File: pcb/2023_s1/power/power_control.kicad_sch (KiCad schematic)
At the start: 21 parts, among them J1 Screw_Terminal_01x05, Q2 TIP122, U1 40106, U3 4N25

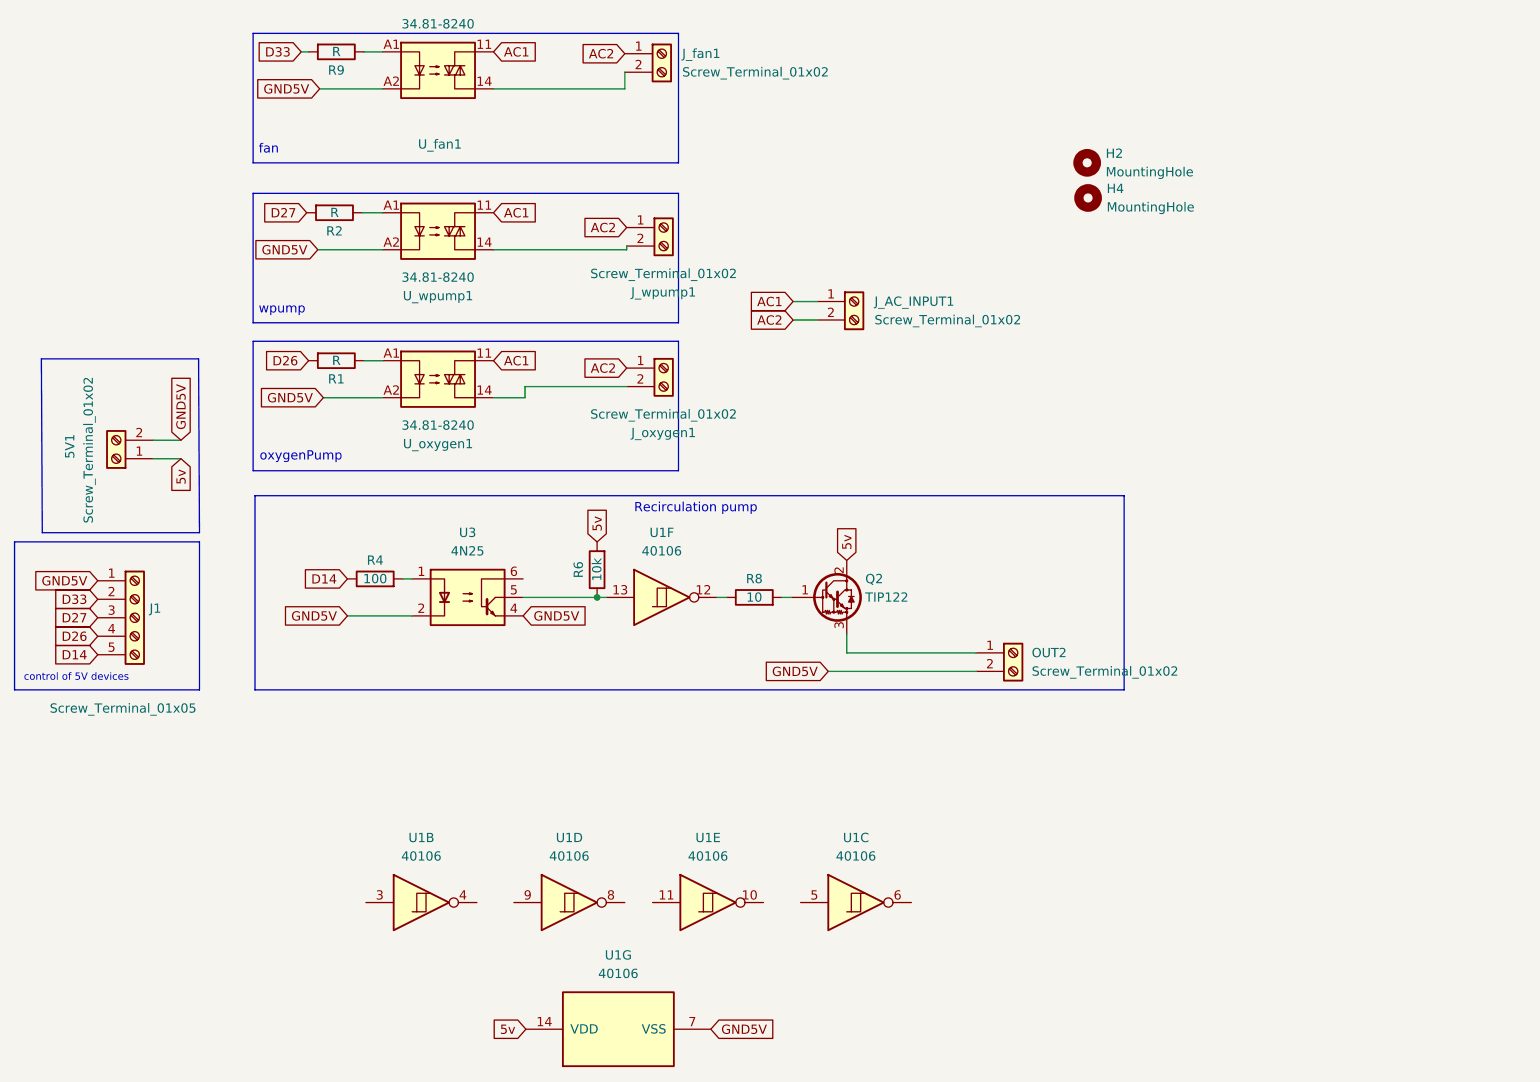
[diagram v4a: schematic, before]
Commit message: update, changed pcbs to use mechanic relays instead of the trigger schmith circuit, because of reliability and simpleness of the design
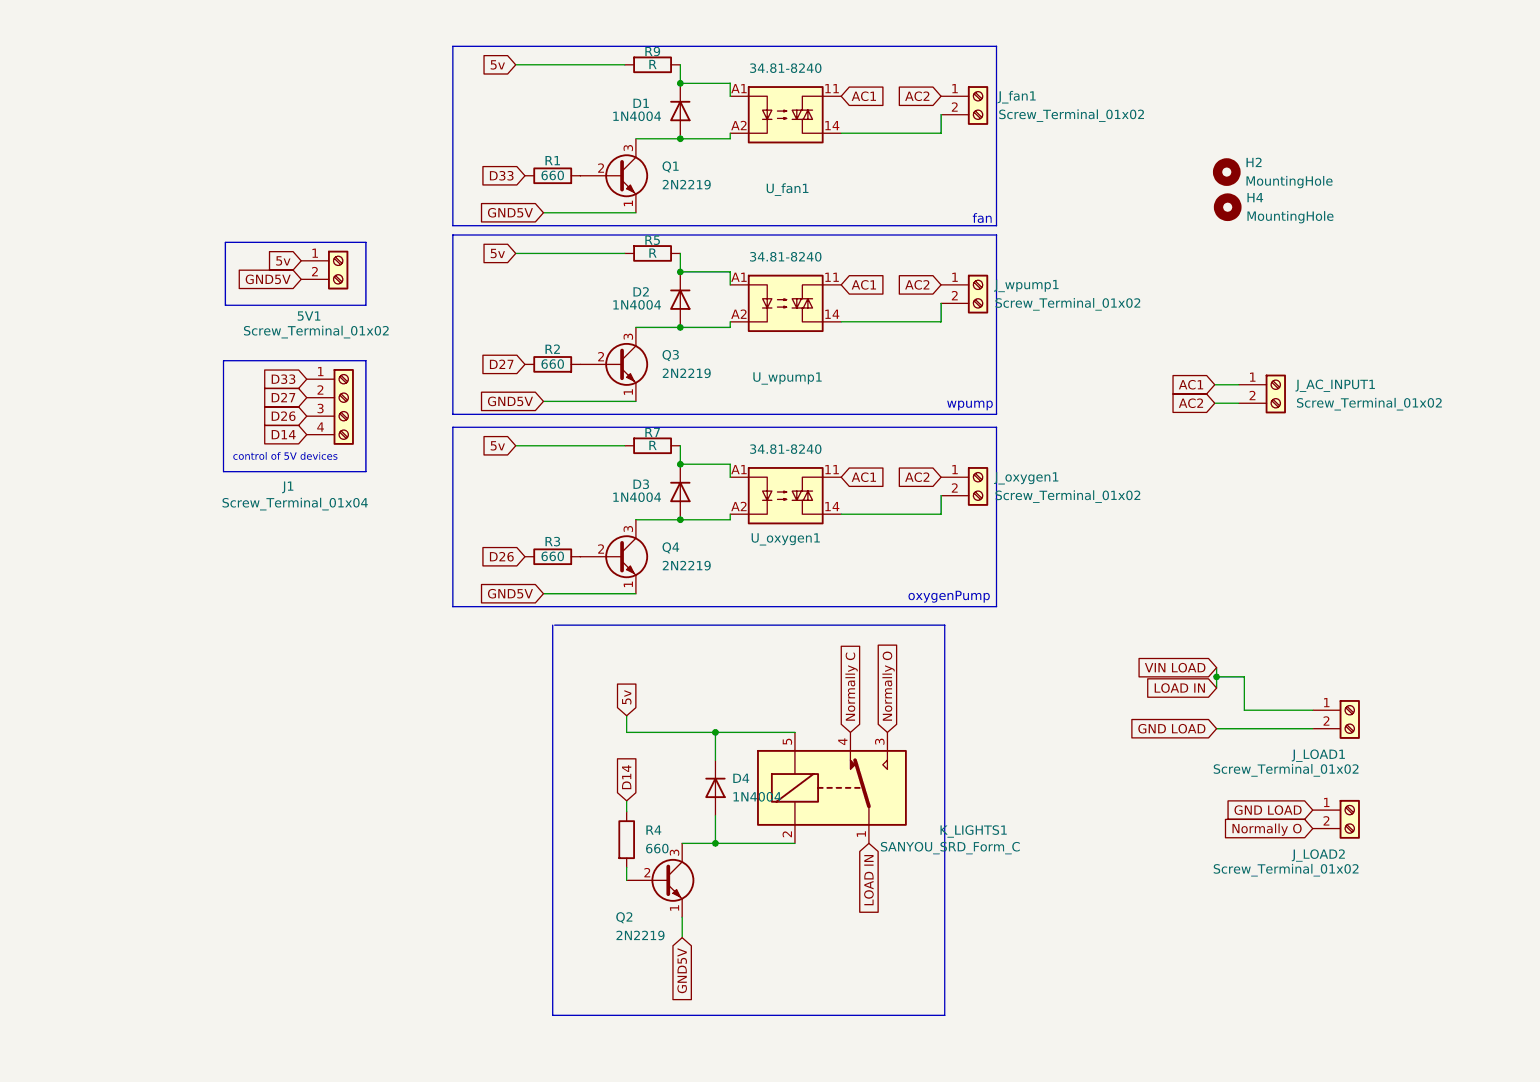
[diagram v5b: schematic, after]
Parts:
- removed J1: Screw_Terminal_01x05, TerminalBlock_Altech:Altech_AK300_1x05_P5.00mm_45-Degree, symbol Connector:Screw_Terminal_01x05
- removed OUT2: Screw_Terminal_01x02, TerminalBlock:TerminalBlock_Altech_AK300-2_P5.00mm, symbol Connector:Screw_Terminal_01x02
- removed Q2: TIP122, Package_TO_SOT_THT:TO-220-3_Vertical, symbol Transistor_BJT:TIP122
- removed R6: 10k, Resistor_THT:R_Axial_DIN0204_L3.6mm_D1.6mm_P2.54mm_Vertical, symbol Device:R
- removed R8: 10, Resistor_THT:R_Axial_DIN0204_L3.6mm_D1.6mm_P2.54mm_Vertical, symbol Device:R
- removed U1: 40106, Package_DIP:DIP-14_W7.62mm, symbol 4xxx:40106
- removed U3: 4N25, Package_DIP:DIP-6_W7.62mm, symbol Isolator:4N25
- added D1, D2, D3, D4: 1N4004, Diode_THT:D_DO-41_SOD81_P10.16mm_Horizontal, symbol Diode:1N4004
- added J1: Screw_Terminal_01x04, TerminalBlock_Altech:Altech_AK300_1x04_P5.00mm_45-Degree, symbol Connector:Screw_Terminal_01x04
- added J_LOAD1, J_LOAD2: Screw_Terminal_01x02, TerminalBlock:TerminalBlock_Altech_AK300-2_P5.00mm, symbol Connector:Screw_Terminal_01x02
- added K_LIGHTS1: SANYOU_SRD_Form_C, Relay_THT:Relay_SPDT_SANYOU_SRD_Series_Form_C, symbol Relay:SANYOU_SRD_Form_C
- added Q1, Q2, Q3, Q4: 2N2219, Package_TO_SOT_THT:TO-39-3, symbol Transistor_BJT:2N2219
- added R3: 660, Resistor_THT:R_Axial_DIN0204_L3.6mm_D1.6mm_P5.08mm_Vertical, symbol Device:R
- added R5, R7: R, Resistor_THT:R_Axial_DIN0204_L3.6mm_D1.6mm_P5.08mm_Vertical, symbol Device:R
- R1, R2: value R -> 660
- R4: value 100 -> 660; footprint Resistor_THT:R_Axial_DIN0204_L3.6mm_D1.6mm_P2.54mm_Vertical -> Resistor_THT:R_Axial_DIN0204_L3.6mm_D1.6mm_P5.08mm_Vertical
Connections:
- net 5v: now also R9.2, D4.1 (K), K_LIGHTS1.5, R5.2, R7.2
- net D14: now also J1.4 (Pin_4)
- net D26: now also J1.3 (Pin_3), R3.1; no longer R1.2
- net D27: now also R2.1, J1.2 (Pin_2); no longer R2.2
- net D33: now also R1.1, J1.1 (Pin_1); no longer R9.2
- net GND5V: now also Q1.1 (E), Q2.1 (E), Q3.1 (E), Q4.1 (E); no longer U_fan1.A2, U_oxygen1.A2, U_wpump1.A2
- net at U_wpump1.A1: now also D2.1 (K), R5.1; no longer R2.1
- net at R9.1, U_fan1.A1: now also D1.1 (K)
- net at U_oxygen1.A1: now also D3.1 (K), R7.1; no longer R1.1
- net at R4.2: now also Q2.2 (B)
- new net: Q3.2 (B), R2.2
- new net: D2.2 (A), Q3.3 (C), U_wpump1.A2
- new net: D3.2 (A), Q4.3 (C), U_oxygen1.A2
- new net: Q1.2 (B), R1.2
- new net: D1.2 (A), Q1.3 (C), U_fan1.A2
- new net: Q4.2 (B), R3.2
- new net: D4.2 (A), K_LIGHTS1.2, Q2.3 (C)
- new net GND LOAD: J_LOAD1.2 (Pin_2), J_LOAD2.1 (Pin_1)
- new net LOAD IN: J_LOAD1.1 (Pin_1), K_LIGHTS1.1
- new net Normally C: K_LIGHTS1.4
- new net Normally O: J_LOAD2.2 (Pin_2), K_LIGHTS1.3
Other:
- note removed: "Recirculation pump"
- moved on the sheet: 5V1, H2, H4, J_AC_INPUT1, J_fan1, R9, U_fan1

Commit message: update
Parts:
- added R6: R, Resistor_THT:R_Axial_DIN0204_L3.6mm_D1.6mm_P5.08mm_Vertical, symbol Device:R
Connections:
- net 5v: now also R6.2; no longer D4.1 (K), K_LIGHTS1.5
- new net: D4.1 (K), K_LIGHTS1.5, R6.1
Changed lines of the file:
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@@
+    (stroke (width 0) (type default) (color 0 0 0 0))
+  )
+  (wire (pts (xy 99.314 111.252) (xy 101.346 111.252))
     (stroke (width 0) (type default) (color 0 0 0 0))
   )
@@
     (stroke (width 0) (type default) (color 0 0 0 0))
   )
+  (wire (pts (xy 108.966 111.252) (xy 111.506 111.252))
+    (stroke (width 0) (type default) (color 0 0 0 0))
+  )
   (polyline (pts (xy 43.942 60.198) (xy 63.5 60.198))
     (stroke (width 0) (type default) (color 0 0 0 0))
@@
   )
   (wire (pts (xy 87.884 39.878) (xy 100.584 39.878))
-    (stroke (width 0) (type default) (color 0 0 0 0))
-  )
-  (wire (pts (xy 99.314 111.252) (xy 111.506 111.252))
     (stroke (width 0) (type default) (color 0 0 0 0))
   )
@@
     (pin "2")
   )
+  (symbol (lib_id "Device:R") (at 105.156 111.252 270) (unit 1)
+    (in_bom yes) (on_board yes)
+    (property "Reference" "R6" (id 0) (at 105.156 109.474 90))
+    (property "Value" "R" (id 1) (at 105.156 111.252 90))
+    (property "Footprint" "Resistor_THT:R_Axial_DIN0204_L3.6mm_D1.6mm_P5.08mm_Vertical" (id 2) (at 105.156 109.474 90)
+      (effects (font (size 1.27 1.27)) hide)
+    )
+    (property "Datasheet" "~" (id 3) (at 105.156 111.252 0)
+      (effects (font (size 1.27 1.27)) hide)
+    )
+    (pin "1")
+    (pin "2")
+  )
   (symbol (lib_id "Diode:1N4004") (at 106.68 25.908 270) (unit 1)
     (in_bom yes) (on_board yes)
@@
       (reference "R5") (unit 1) (value "R") (footprint "Resistor_THT:R_Axial_DIN0204_L3.6mm_D1.6mm_P5.08mm_Vertical")
     )
+    (path "/c6724451-d400-4fc5-8595-c729cb240f8d"
+      (reference "R6") (unit 1) (value "R") (footprint "Resistor_THT:R_Axial_DIN0204_L3.6mm_D1.6mm_P5.08mm_Vertical")
+    )
     (path "/77a1f621-1615-47ac-86a4-1ee5cc2fe8e6"
